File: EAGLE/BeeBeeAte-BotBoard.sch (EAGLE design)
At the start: 104 parts, among them IC1 CP2102, J1 3-1734035-2, T1 S8050, T2 S8050, U1 ESP32-WROOM-32, U2 LM5.0, U3 DRIVER 2, U4 DRIVER 1, U5 DRIVER 3, U6 DRIVER 4

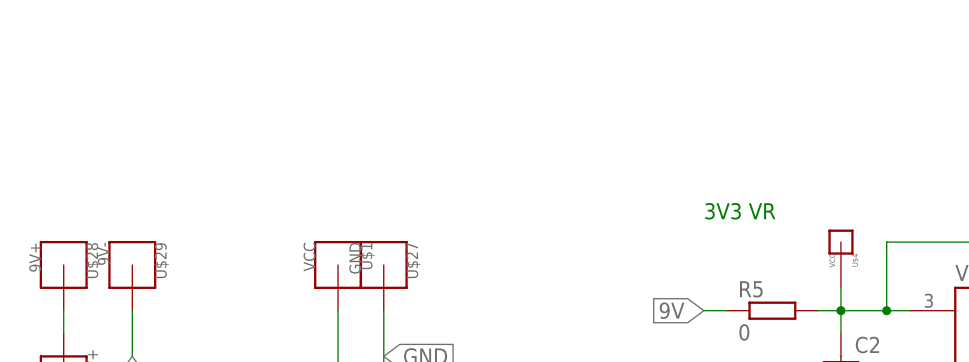
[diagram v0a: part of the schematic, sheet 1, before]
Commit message: Added Motors
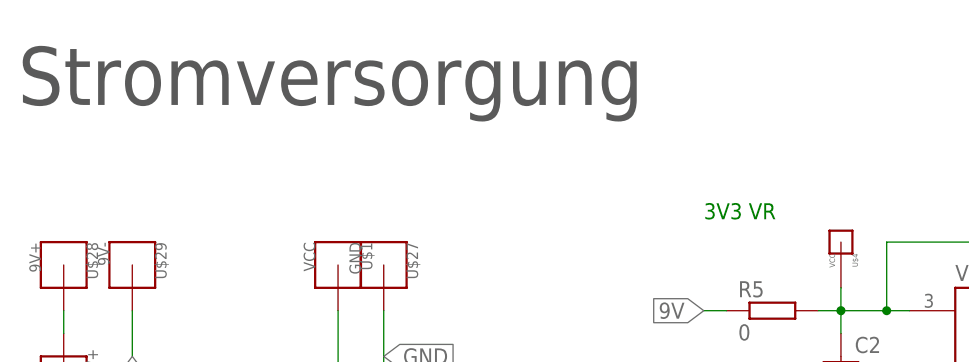
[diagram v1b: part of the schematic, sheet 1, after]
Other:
- note added: "ESP32 und USB-Modul"
- note added: "MPU6050"
- note added: "Motoren Treiber"
- note added: "Stromversorgung"
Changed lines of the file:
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@@
 <text x="111.76" y="83.82" size="1.778" layer="91">5V VR</text>
 <text x="114.3" y="124.46" size="1.778" layer="91">3V3 VR</text>
+<text x="38.1" y="137.16" size="6.4516" layer="97">Stromversorgung</text>
 </plain>
 <instances>
@@
 <text x="147.32" y="119.38" size="1.778" layer="150">D3 weglassen</text>
 <text x="147.32" y="116.84" size="1.778" layer="150">Eventuell 0Ohm</text>
+<text x="45.72" y="167.64" size="6.4516" layer="97">ESP32 und USB-Modul</text>
 </plain>
 <instances>
@@
 <description>Treiber für Motoren</description>
 <plain>
+<text x="27.94" y="139.7" size="6.4516" layer="97">Motoren Treiber</text>
 </plain>
 <instances>
@@
 <description>MPU6050</description>
 <plain>
+<text x="91.44" y="127" size="6.4516" layer="97">MPU6050</text>
 </plain>
 <instances>
